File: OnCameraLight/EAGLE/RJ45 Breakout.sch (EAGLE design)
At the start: 7 parts, among them J1 RJHSE-5381

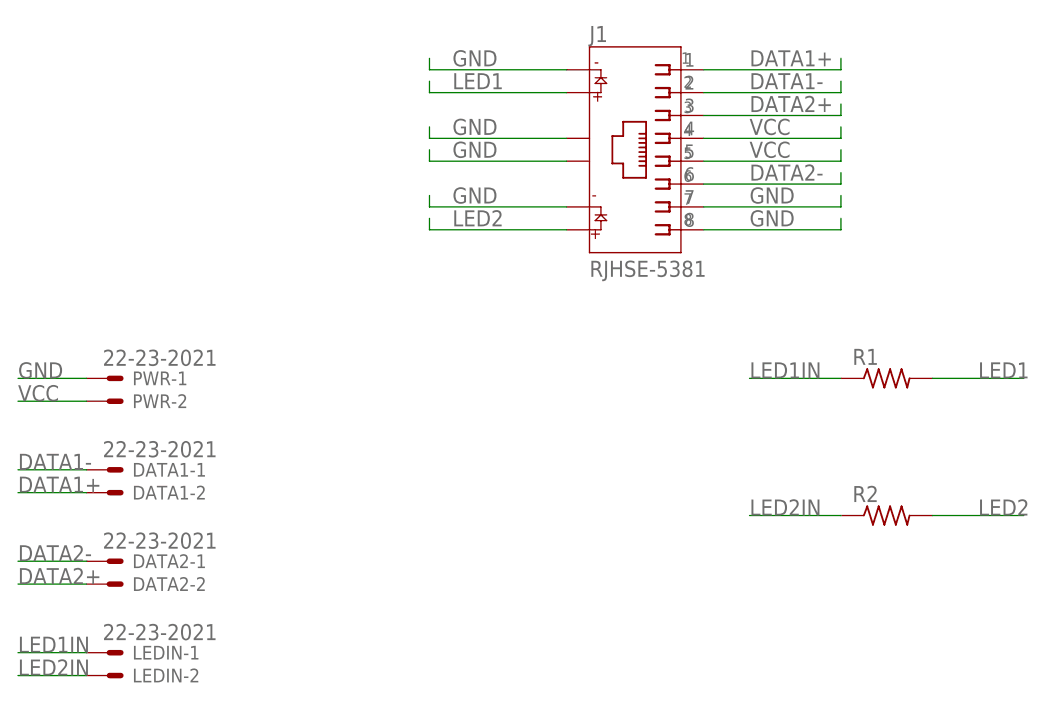
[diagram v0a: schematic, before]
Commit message: Go through and fix notation on RS485 wiring everywhere to use the standard A/B notation.
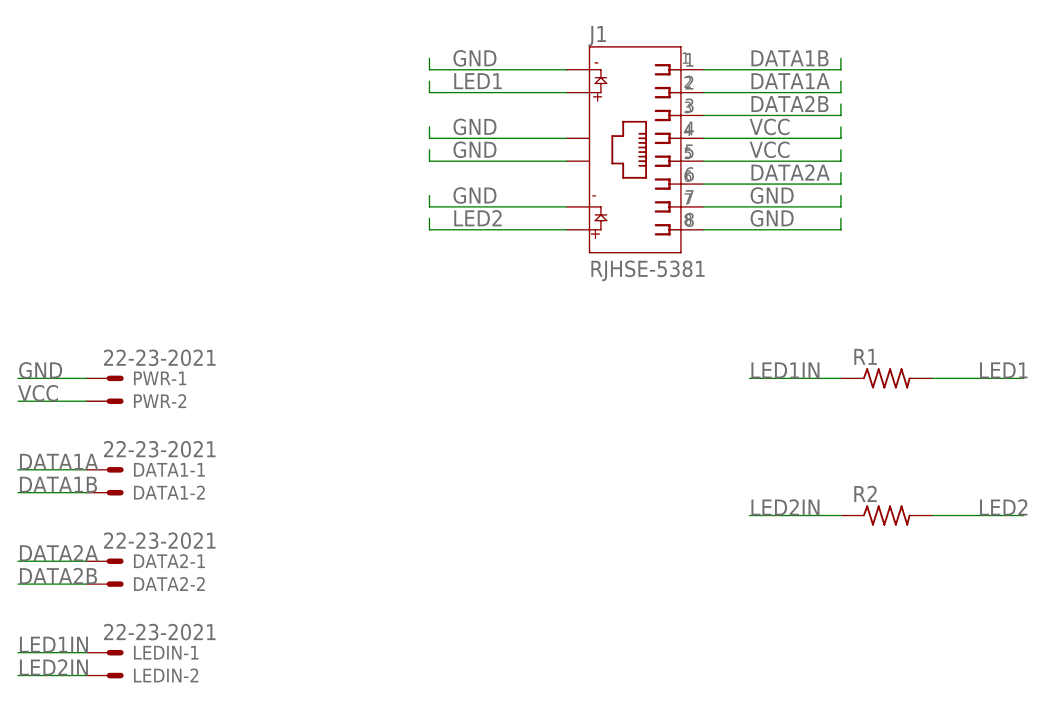
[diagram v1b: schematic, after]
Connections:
- net DATA1+ renamed DATA1B
- net DATA1- renamed DATA1A
- net DATA2+ renamed DATA2B
- net DATA2- renamed DATA2A
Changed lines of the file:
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@@
-</segment>
-</net>
-<net name="DATA2-" class="0">
-<segment>
-<pinref part="DATA2" gate="-1" pin="S"/>
-<wire x1="40.64" y1="73.66" x2="33.02" y2="73.66" width="0.1524" layer="91"/>
-<label x="33.02" y="73.66" size="1.778" layer="95"/>
-</segment>
-<segment>
-<pinref part="J1" gate="G$1" pin="6"/>
-<wire x1="109.22" y1="115.57" x2="124.46" y2="115.57" width="0.1524" layer="91"/>
-<wire x1="124.46" y1="115.57" x2="124.46" y2="116.84" width="0.1524" layer="91"/>
-<label x="114.3" y="116.84" size="1.778" layer="95" align="center-left"/>
-</segment>
-</net>
-<net name="DATA1+" class="0">
-<segment>
-<pinref part="DATA1" gate="-2" pin="S"/>
-<wire x1="40.64" y1="81.28" x2="33.02" y2="81.28" width="0.1524" layer="91"/>
-<label x="33.02" y="81.28" size="1.778" layer="95"/>
-</segment>
-<segment>
-<pinref part="J1" gate="G$1" pin="1"/>
-<wire x1="109.22" y1="128.27" x2="124.46" y2="128.27" width="0.1524" layer="91"/>
-<wire x1="124.46" y1="128.27" x2="124.46" y2="129.54" width="0.1524" layer="91"/>
-<label x="114.3" y="129.54" size="1.778" layer="95" align="center-left"/>
-</segment>
-</net>
-<net name="DATA2+" class="0">
-<segment>
-<pinref part="DATA2" gate="-2" pin="S"/>
-<wire x1="40.64" y1="71.12" x2="33.02" y2="71.12" width="0.1524" layer="91"/>
-<label x="33.02" y="71.12" size="1.778" layer="95"/>
-</segment>
-<segment>
-<pinref part="J1" gate="G$1" pin="3"/>
-<wire x1="109.22" y1="123.19" x2="124.46" y2="123.19" width="0.1524" layer="91"/>
-<wire x1="124.46" y1="123.19" x2="124.46" y2="124.46" width="0.1524" layer="91"/>
-<label x="114.3" y="124.46" size="1.778" layer="95" align="center-left"/>
-</segment>
-</net>
-<net name="DATA1-" class="0">
-<segment>
-<pinref part="DATA1" gate="-1" pin="S"/>
-<wire x1="40.64" y1="83.82" x2="33.02" y2="83.82" width="0.1524" layer="91"/>
-<label x="33.02" y="83.82" size="1.778" layer="95"/>
-</segment>
-<segment>
-<pinref part="J1" gate="G$1" pin="2"/>
-<wire x1="109.22" y1="125.73" x2="124.46" y2="125.73" width="0.1524" layer="91"/>
-<wire x1="124.46" y1="125.73" x2="124.46" y2="127" width="0.1524" layer="91"/>
-<label x="114.3" y="127" size="1.778" layer="95" align="center-left"/>
 </segment>
 </net>
@@
 </segment>
 </net>
+<net name="DATA1B" class="0">
+<segment>
+<pinref part="J1" gate="G$1" pin="1"/>
+<wire x1="109.22" y1="128.27" x2="124.46" y2="128.27" width="0.1524" layer="91"/>
+<wire x1="124.46" y1="128.27" x2="124.46" y2="129.54" width="0.1524" layer="91"/>
+<label x="114.3" y="129.54" size="1.778" layer="95" align="center-left"/>
+</segment>
+<segment>
+<pinref part="DATA1" gate="-2" pin="S"/>
+<wire x1="40.64" y1="81.28" x2="33.02" y2="81.28" width="0.1524" layer="91"/>
+<label x="33.02" y="81.28" size="1.778" layer="95"/>
+</segment>
+</net>
+<net name="DATA1A" class="0">
+<segment>
+<pinref part="J1" gate="G$1" pin="2"/>
+<wire x1="109.22" y1="125.73" x2="124.46" y2="125.73" width="0.1524" layer="91"/>
+<wire x1="124.46" y1="125.73" x2="124.46" y2="127" width="0.1524" layer="91"/>
+<label x="114.3" y="127" size="1.778" layer="95" align="center-left"/>
+</segment>
+<segment>
+<pinref part="DATA1" gate="-1" pin="S"/>
+<wire x1="40.64" y1="83.82" x2="33.02" y2="83.82" width="0.1524" layer="91"/>
+<label x="33.02" y="83.82" size="1.778" layer="95"/>
+</segment>
+</net>
+<net name="DATA2B" class="0">
+<segment>
+<pinref part="J1" gate="G$1" pin="3"/>
+<wire x1="109.22" y1="123.19" x2="124.46" y2="123.19" width="0.1524" layer="91"/>
+<wire x1="124.46" y1="123.19" x2="124.46" y2="124.46" width="0.1524" layer="91"/>
+<label x="114.3" y="124.46" size="1.778" layer="95" align="center-left"/>
+</segment>
+<segment>
+<pinref part="DATA2" gate="-2" pin="S"/>
+<wire x1="40.64" y1="71.12" x2="33.02" y2="71.12" width="0.1524" layer="91"/>
+<label x="33.02" y="71.12" size="1.778" layer="95"/>
+</segment>
+</net>
+<net name="DATA2A" class="0">
+<segment>
+<pinref part="J1" gate="G$1" pin="6"/>
+<wire x1="109.22" y1="115.57" x2="124.46" y2="115.57" width="0.1524" layer="91"/>
+<wire x1="124.46" y1="115.57" x2="124.46" y2="116.84" width="0.1524" layer="91"/>
+<label x="114.3" y="116.84" size="1.778" layer="95" align="center-left"/>
+</segment>
+<segment>
+<pinref part="DATA2" gate="-1" pin="S"/>
+<wire x1="40.64" y1="73.66" x2="33.02" y2="73.66" width="0.1524" layer="91"/>
+<label x="33.02" y="73.66" size="1.778" layer="95"/>
+</segment>
+</net>
